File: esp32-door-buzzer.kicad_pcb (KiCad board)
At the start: 2 copper layers, 11 parts, among them J1 ESP32-S3, J2 ESP32-S3, J3 Conn_01x06_Pin, J4 Conn_01x02_Pin, K1 HK4100F-DC5V-SHG, Q1 NPN, U1 Optocoupler_DC_PhotoNPN_AKEC, U2 L78L12_TO92

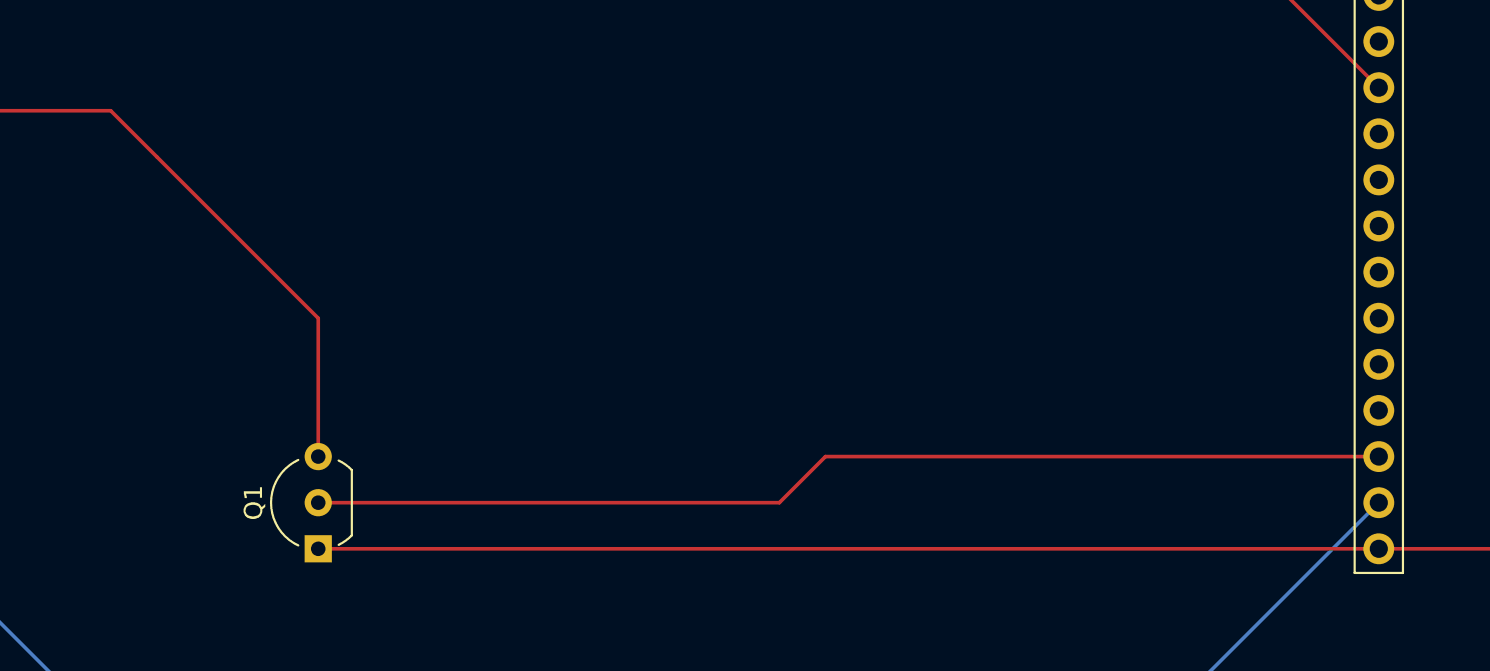
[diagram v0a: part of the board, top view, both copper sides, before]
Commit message: Change transistor to a mosfet
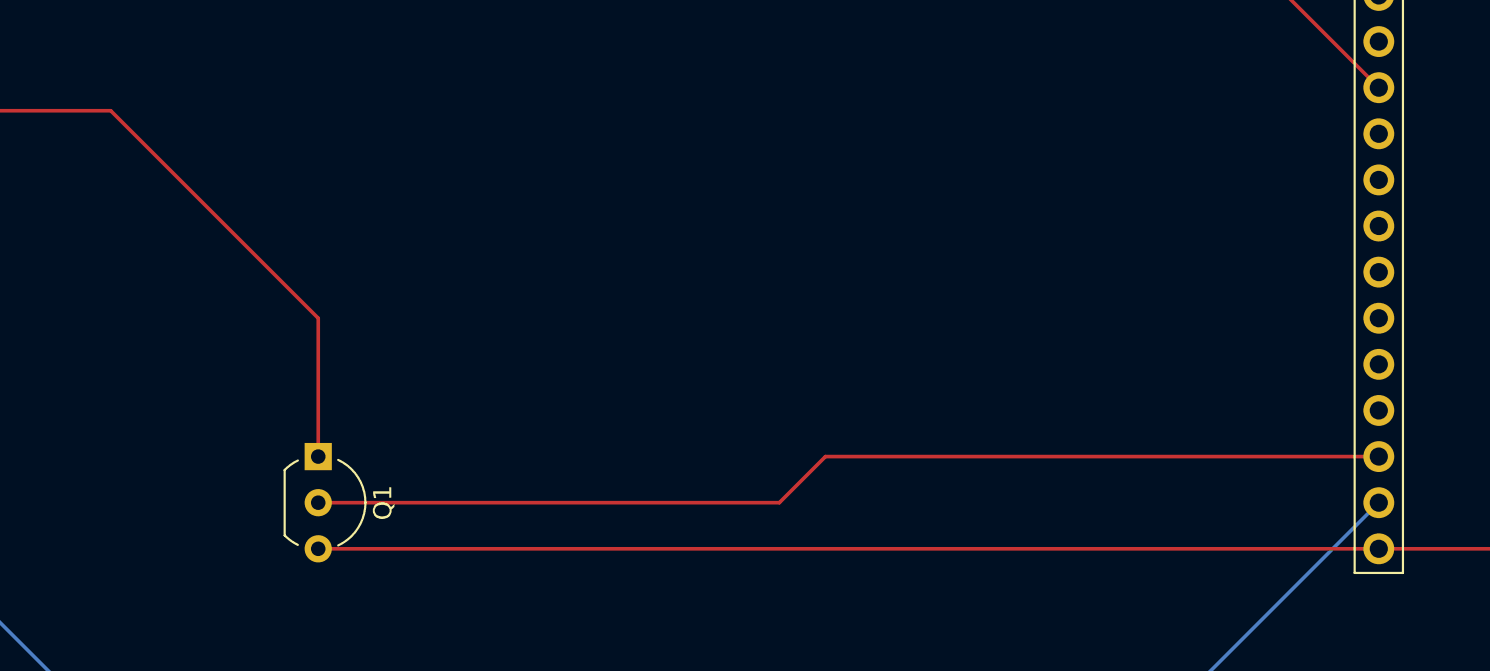
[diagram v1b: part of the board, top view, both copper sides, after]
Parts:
- Q1: value NPN -> NMOS
- moved Q1 5.08 mm to (167.6, 114.3), turned to -90 degrees
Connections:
- Q1 pad 1: GND -> Net-(D2-A)
- Q1 pad 3: Net-(D2-A) -> GND
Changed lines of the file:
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@@
 	(footprint "Package_TO_SOT_THT:TO-92_Inline_Wide"
 		(layer "F.Cu")
-		(at 167.64 119.38 90)
+		(at 167.64 114.3 -90)
 		(descr "TO-92 leads in-line, wide, drill 0.75mm (see NXP sot054_po.pdf)")
 		(tags "to-92 sc-43 sc-43a sot54 PA33 transistor")
@@
 			)
 		)
-		(property "Value" "NPN"
+		(property "Value" "NMOS"
 			(at 2.54 2.79 90)
 			(layer "F.Fab")
@@
 			)
 		)
-		(property "Datasheet" "https://ngspice.sourceforge.io/docs/ngspice-html-manual/manual.xhtml#cha_BJTs"
-			(at 0 0 90)
+		(property "Datasheet" "https://ngspice.sourceforge.io/docs/ngspice-html-manual/manual.xhtml#cha_MOSFETs"
+			(at 0 0 270)
 			(unlocked yes)
 			(layer "F.Fab")
@@
 			)
 		)
-		(property "Description" "Bipolar transistor symbol for simulation only, substrate tied to the emitter"
-			(at 0 0 90)
+		(property "Description" "N-MOSFET transistor, drain/source/gate"
+			(at 0 0 270)
 			(unlocked yes)
 			(layer "F.Fab")
@@
 			)
 		)
-		(property "Sim.Device" "NPN"
-			(at 0 0 90)
+		(property "Sim.Device" "NMOS"
+			(at 0 0 270)
 			(unlocked yes)
 			(layer "F.Fab")
@@
 			)
 		)
-		(property "Sim.Type" "GUMMELPOON"
-			(at 0 0 90)
+		(property "Sim.Type" "VDMOS"
+			(at 0 0 270)
 			(unlocked yes)
 			(layer "F.Fab")
@@
 			)
 		)
-		(property "Sim.Pins" "1=C 2=B 3=E"
-			(at 0 0 90)
+		(property "Sim.Pins" "1=D 2=G 3=S"
+			(at 0 0 270)
 			(unlocked yes)
 			(layer "F.Fab")
@@
 			(start 0.74 1.85)
 			(end 4.34 1.85)
+			(stroke
+				(width 0.12)
+				(type solid)
+			)
+			(layer "F.SilkS")
+		)
+		(fp_arc
+			(start 0.74 1.85)
+			(mid 0.446097 1.509328)
+			(end 0.215816 1.122795)
+			(stroke
+				(width 0.12)
+				(type solid)
+			)
+			(layer "F.SilkS")
+		)
+		(fp_arc
+			(start 4.864184 1.122795)
+			(mid 4.633903 1.509328)
+			(end 4.34 1.85)
+			(stroke
+				(width 0.12)
+				(type solid)
+			)
+			(layer "F.SilkS")
+		)
+		(fp_arc
+			(start 0.1836 -1.098807)
+			(mid 1.143021 -2.192817)
+			(end 2.54 -2.6)
 			(stroke
 				(width 0.12)
@@
 			(layer "F.SilkS")
 		)
-		(fp_arc
-			(start 0.1836 -1.098807)
-			(mid 1.143021 -2.192817)
-			(end 2.54 -2.6)
-			(stroke
-				(width 0.12)
-				(type solid)
-			)
-			(layer "F.SilkS")
-		)
-		(fp_arc
-			(start 4.864184 1.122795)
-			(mid 4.633903 1.509328)
-			(end 4.34 1.85)
-			(stroke
-				(width 0.12)
-				(type solid)
-			)
-			(layer "F.SilkS")
-		)
-		(fp_arc
-			(start 0.74 1.85)
-			(mid 0.446097 1.509328)
-			(end 0.215816 1.122795)
-			(stroke
-				(width 0.12)
-				(type solid)
-			)
-			(layer "F.SilkS")
+		(fp_line
+			(start 6.09 2.01)
+			(end -1.01 2.01)
+			(stroke
+				(width 0.05)
+				(type solid)
+			)
+			(layer "F.CrtYd")
+		)
+		(fp_line
+			(start 6.09 2.01)
+			(end 6.09 -2.73)
+			(stroke
+				(width 0.05)
+				(type solid)
+			)
+			(layer "F.CrtYd")
+		)
+		(fp_line
+			(start -1.01 -2.73)
+			(end -1.01 2.01)
+			(stroke
+				(width 0.05)
+				(type solid)
+			)
+			(layer "F.CrtYd")
 		)
 		(fp_line
@@
 		)
 		(fp_line
-			(start -1.01 -2.73)
-			(end -1.01 2.01)
-			(stroke
-				(width 0.05)
-				(type solid)
-			)
-			(layer "F.CrtYd")
-		)
-		(fp_line
-			(start 6.09 2.01)
-			(end 6.09 -2.73)
-			(stroke
-				(width 0.05)
-				(type solid)
-			)
-			(layer "F.CrtYd")
-		)
-		(fp_line
-			(start 6.09 2.01)
-			(end -1.01 2.01)
-			(stroke
-				(width 0.05)
-				(type solid)
-			)
-			(layer "F.CrtYd")
-		)
-		(fp_line
 			(start 0.8 1.75)
 			(end 4.3 1.75)
+			(stroke
+				(width 0.1)
+				(type solid)
+			)
+			(layer "F.Fab")
+		)
+		(fp_arc
+			(start 0.786375 1.753625)
+			(mid 0.248779 -0.949055)
+			(end 2.54 -2.48)
 			(stroke
 				(width 0.1)
@@
 			(layer "F.Fab")
 		)
-		(fp_arc
-			(start 0.786375 1.753625)
-			(mid 0.248779 -0.949055)
-			(end 2.54 -2.48)
-			(stroke
-				(width 0.1)
-				(type solid)
-			)
-			(layer "F.Fab")
-		)
 		(fp_text user "${REFERENCE}"
 			(at 2.54 0 90)
@@
 		)
 		(pad "1" thru_hole rect
-			(at 0 0 90)
+			(at 0 0 270)
 			(size 1.5 1.5)
 			(drill 0.8)
 			(layers "*.Cu" "*.Mask")
 			(remove_unused_layers no)
-			(net 7 "GND")
-			(pinfunction "E")
-			(pintype "open_emitter")
+			(net 4 "Net-(D2-A)")
+			(pinfunction "D")
+			(pintype "passive")
 		)
 		(pad "2" thru_hole circle
-			(at 2.54 0 90)
+			(at 2.54 0 270)
 			(size 1.5 1.5)
 			(drill 0.8)
@@
 			(remove_unused_layers no)
 			(net 13 "/GPIO12")
-			(pinfunction "B")
+			(pinfunction "G")
 			(pintype "input")
 		)
 		(pad "3" thru_hole circle
-			(at 5.08 0 90)
+			(at 5.08 0 270)
 			(size 1.5 1.5)
 			(drill 0.8)
 			(layers "*.Cu" "*.Mask")
 			(remove_unused_layers no)
-			(net 4 "Net-(D2-A)")
-			(pinfunction "C")
-			(pintype "open_collector")
+			(net 7 "GND")
+			(pinfunction "S")
+			(pintype "passive")
 		)
 		(embedded_fonts no)
@@
 	)
 	(segment
+		(start 113.03 95.25)
+		(end 156.21 95.25)
+		(width 0.2)
+		(layer "F.Cu")
+		(net 4)
+	)
+	(segment
 		(start 109.22 99.06)
 		(end 113.03 95.25)
@@
 	)
 	(segment
+		(start 156.21 95.25)
+		(end 167.64 106.68)
+		(width 0.2)
+		(layer "F.Cu")
+		(net 4)
+	)
+	(segment
 		(start 167.64 106.68)
 		(end 167.64 114.3)
@@
 	)
 	(segment
-		(start 113.03 95.25)
-		(end 156.21 95.25)
-		(width 0.2)
-		(layer "F.Cu")
-		(net 4)
-	)
-	(segment
-		(start 156.21 95.25)
-		(end 158.75 97.79)
-		(width 0.2)
-		(layer "F.Cu")
-		(net 4)
-	)
-	(segment
-		(start 158.75 97.79)
-		(end 167.64 106.68)
-		(width 0.2)
-		(layer "F.Cu")
-		(net 4)
-	)
-	(segment
 		(start 107.95 109.22)
 		(end 104.14 105.41)
@@
 	)
 	(segment
+		(start 254 76.2)
+		(end 254 109.22)
+		(width 0.2)
+		(layer "F.Cu")
+		(net 7)
+	)
+	(segment
+		(start 254 109.22)
+		(end 248.92 114.3)
+		(width 0.2)
+		(layer "F.Cu")
+		(net 7)
+	)
+	(segment
 		(start 167.64 119.38)
 		(end 226.06 119.38)
@@
 	)
 	(segment
-		(start 254 76.2)
-		(end 254 109.22)
-		(width 0.2)
-		(layer "F.Cu")
-		(net 7)
-	)
-	(segment
-		(start 254 109.22)
-		(end 248.92 114.3)
-		(width 0.2)
-		(layer "F.Cu")
-		(net 7)
-	)
-	(segment
 		(start 248.92 114.3)
 		(end 248.92 116.84)
@@
 	)
 	(segment
+		(start 193.04 116.84)
+		(end 195.58 114.3)
+		(width 0.2)
+		(layer "F.Cu")
+		(net 13)
+	)
+	(segment
 		(start 195.58 114.3)
+		(end 226.06 114.3)
+		(width 0.2)
+		(layer "F.Cu")
+		(net 13)
+	)
+	(segment
+		(start 167.64 116.84)
 		(end 193.04 116.84)
 		(width 0.2)
 		(layer "F.Cu")
-		(net 13)
-	)
-	(segment
-		(start 226.06 114.3)
-		(end 195.58 114.3)
-		(width 0.2)
-		(layer "F.Cu")
-		(net 13)
-	)
-	(segment
-		(start 193.04 116.84)
-		(end 167.64 116.84)
-		(width 0.2)
-		(layer "F.Cu")
